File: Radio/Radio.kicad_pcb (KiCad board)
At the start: 2 copper layers, 12 parts, among them J1 USB_B_Micro, U1 FT231XS, U2 XBee_SMT

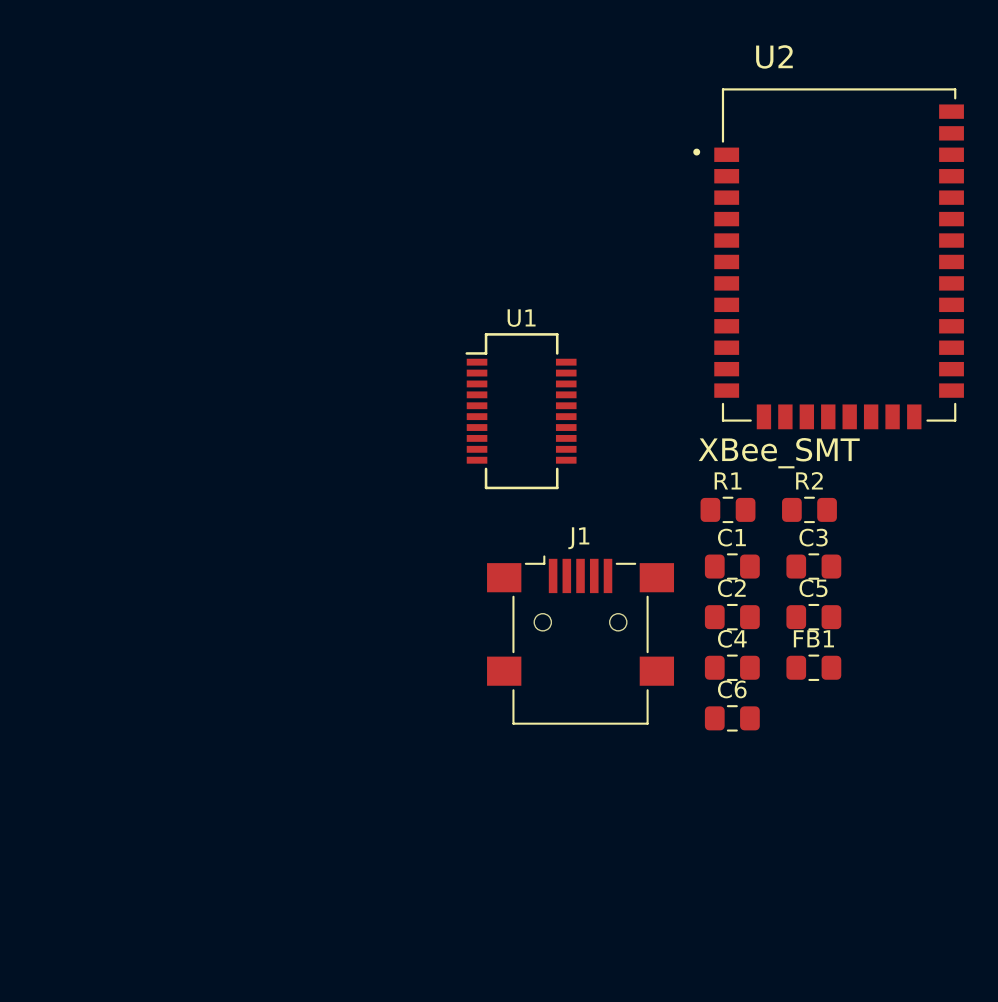
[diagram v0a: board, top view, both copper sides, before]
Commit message: Added proper xbee footprint, did initial layout
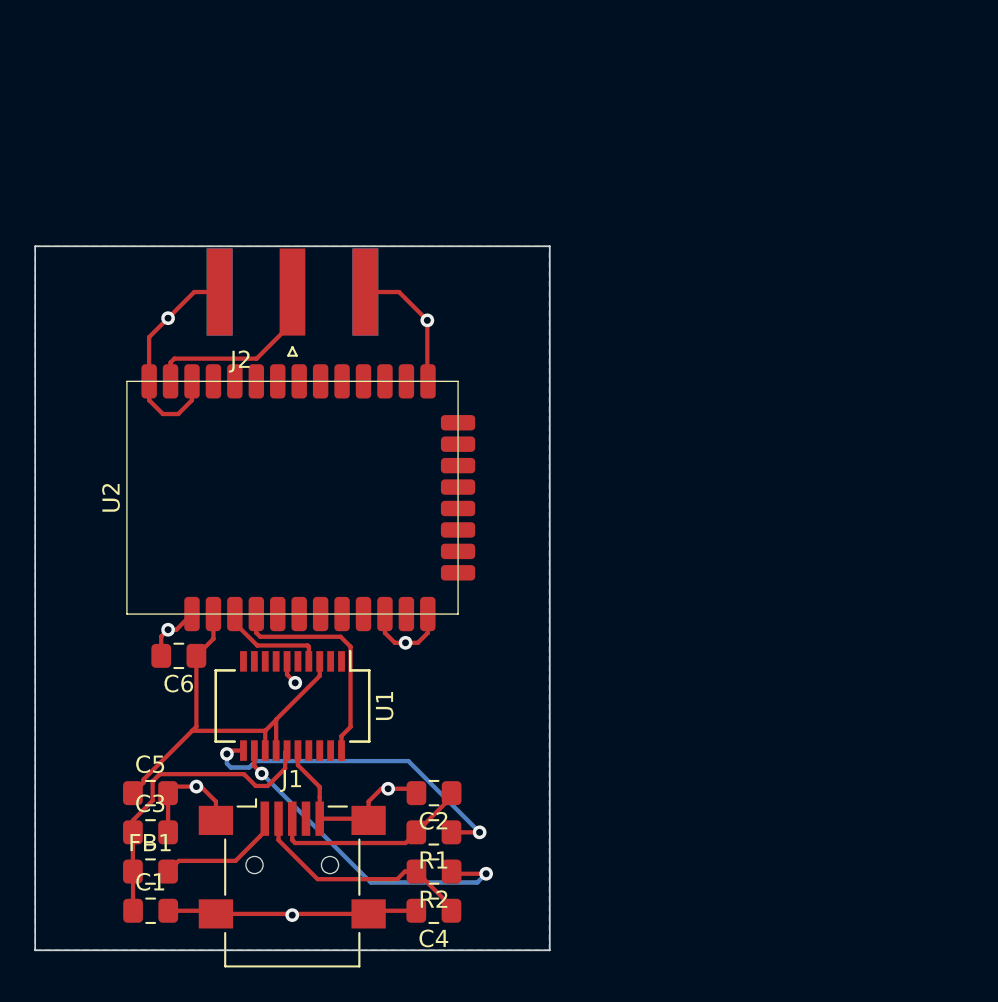
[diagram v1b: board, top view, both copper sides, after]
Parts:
- added J2: Conn_Coaxial, Connector_Coaxial:SMA_Amphenol_132289_EdgeMount, F.Cu at (150.0, 71.6)
- U2: value XBee_SMT -> XB3; footprint XB3-24Z8CM-J:XCVR_XB3-24Z8CM-J -> Radio:XB3-24Z8RM-J
- moved C3 41.7 mm to (141.7, 103.1)
- moved FB1 40.5 mm to (141.7, 105.4)
- moved C5 40.0 mm to (141.7, 100.8)
- moved C1 39.4 mm to (141.7, 107.7)
- moved U2 34.9 mm to (150.0, 83.6), turned to 90 degrees
- moved C6 32.5 mm to (143.4, 92.8), turned to 180 degrees
- moved R2 30.4 mm to (158.3, 105.4), turned to 180 degrees
- moved R1 25.4 mm to (158.2, 103.1), turned to 180 degrees
- moved C4 22.4 mm to (158.2, 107.7), turned to 180 degrees
- moved J1 22.0 mm to (150.0, 105.0)
- moved U1 21.8 mm to (150.0, 95.8), turned to 270 degrees
- moved C2 20.2 mm to (158.3, 100.8), turned to 180 degrees
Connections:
- U2 pad 10: Net-(U2-Pad10) -> GND
- U2 pad 11: GND -> Net-(U2-Pad11)
- U2 pad 12: Net-(U2-Pad12) -> GND
- U2 pad 13: GND -> Net-(U2-Pad13)
- U2 pad 17: Net-(U2-Pad17) -> (no net)
- U2 pad 18: Net-(U2-Pad18) -> (no net)
- U2 pad 19: Net-(U2-Pad19) -> (no net)
- U2 pad 20: Net-(U2-Pad20) -> (no net)
- U2 pad 21: Net-(U2-Pad21) -> GND
- U2 pad 22: GND -> (no net)
- U2 pad 32: Net-(U2-Pad32) -> GND
- U2 pad 34: Net-(U2-Pad34) -> GND
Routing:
- net GND: track 0.00 -> 65.4 mm, vias 0 -> 8
- net +3V3: track 0.00 -> 25.0 mm
- net Net-(R1-Pad1): track 0.00 -> 20.0 mm, vias 0 -> 2
- net Net-(R2-Pad1): track 0.00 -> 19.5 mm, vias 0 -> 2
- net VBUS: track 0.00 -> 17.7 mm
- net Net-(C4-Pad1): track 0.00 -> 13.5 mm
- net Net-(U1-Pad20): track 0.00 -> 13.2 mm
- net Net-(C2-Pad1): track 0.00 -> 11.9 mm
- net Net-(J2-Pad1): track 0.00 -> 11.0 mm
- net Net-(FB1-Pad2): track 0.00 -> 7.35 mm
- net Net-(U1-Pad4): track 0.00 -> 6.26 mm
- added copper zone on B.Cu, net GND
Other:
- board outline added: 30 x 41 mm

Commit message: Revised layout significantly
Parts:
- added C7: 8.2pf, Capacitor_SMD:C_0805_2012Metric_Pad1.15x1.40mm_HandSolder, F.Cu at (143.4, 96.9)
- added C8: 1uF, Capacitor_SMD:C_0805_2012Metric_Pad1.15x1.40mm_HandSolder, F.Cu at (143.4, 94.9)
- moved J2 2.79 mm to (150.0, 68.8)
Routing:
- net GND: track 65.4 -> 81.6 mm, vias 8 -> 9
- net Net-(J2-Pad1): track 11.0 -> 12.3 mm
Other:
- board size 30 x 41 mm -> 30 x 43.8 mm
- net class Default: clearance 0.2 -> 0.127; trace_width 0.25 -> 0.2; via_dia 0.8 -> 0.6
- net class Power added: clearance 0.2, trace_width 0.4, via_dia 0.6, via_drill 0.4
- rule trace_clearance: 0.2 -> 0.127
- board text added: "RMTS Receiver"
- board text added: "Rev 1"
